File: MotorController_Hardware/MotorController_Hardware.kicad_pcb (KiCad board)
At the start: 2 copper layers, 124.5 x 150.9 mm, 243 parts, among them Q12 Q_NMOS_DGS, Q13 Q_NMOS_DGS, Q14 Q_NMOS_DGS, Q15 Q_NMOS_DGS, Q16 Q_NMOS_DGS, Q17 Q_NMOS_DGS, Q4 Q_NMOS_DGS, Q5 Q_NMOS_DGS, Q6 Q_NMOS_DGS, Q7 Q_NMOS_DGS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

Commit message: CDR Layout changes
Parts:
- added REF**: 4_40_Hole, MRDT_Drill_Holes:4_40_Hole_Corner, B.Cu at (58.6, -34.4)
- added REF**: 4_40_Hole, MRDT_Drill_Holes:4_40_Hole_Corner, B.Cu at (167.0, -34.4)
- D10, D11, D12, D16, D17, D18, D19, D20, D21, D7, D8, D9: value D_Zener -> 15V
- Q12, Q13, Q14, Q15, Q16, Q17, Q4, Q5, Q6, Q7, Q8, Q9: value Q_NMOS_DGS -> FQP30N06L
- R10, R81: value 2k -> 1.5K
- R14, R78: footprint Resistors_SMD:R_0603_HandSoldering -> Resistors_SMD:R_1206_HandSoldering
- U2, U6: moved to F.Cu
- U3: footprint MotorController_Hardware:LAUNCHXL_F28069M_Launchpad_FULL_Booster_SMD_Top -> MRDT_Shields:LAUNCHXL_F28069M_Launchpad_FULL_Booster_SMD_Bottom
- moved C37 57.7 mm to (54.9, -21.1), turned to 0 degrees
- moved C9 50.6 mm to (54.6, 0.25)
- moved C7 49.0 mm to (170.7, -18.5), turned to 180 degrees
- moved C45 48.7 mm to (170.9, 2.79)
- moved C5 43.3 mm to (157.2, -19.8), turned to 180 degrees
- moved C39 35.9 mm to (157.2, 1.52), turned to 180 degrees
- moved C38 33.5 mm to (68.3, -22.4), turned to 0 degrees
- moved C36 33.4 mm to (68.4, -1.02), turned to 0 degrees
- moved R69 24.8 mm to (119.5, -29.0), turned to 0 degrees
- moved R71 24.8 mm to (119.5, -7.62), turned to 0 degrees
- moved R73 24.8 mm to (119.5, 13.7), turned to 0 degrees
- moved R37 24.6 mm to (105.7, -34.5), turned to 180 degrees
- moved R67 24.6 mm to (105.7, 8.13), turned to 180 degrees
- moved R68 24.6 mm to (119.5, -39.6), turned to 0 degrees
- moved R70 24.6 mm to (119.5, -18.3), turned to 0 degrees
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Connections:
- C42 pad 1: +3V3 -> GND
- C42 pad 2: GND -> +3V3
- C65 pad 1: GND -> Net-(C65-Pad1)
- C65 pad 2: Net-(C65-Pad2) -> GND
- C66 pad 1: GND -> Net-(C66-Pad1)
- C66 pad 2: Net-(C66-Pad2) -> GND
- Conn1 pad 1: SL_TX_M1 -> SL_TX
- Conn1 pad 2: SL_RX_M1 -> SL_RX
- Conn1 pad 3: SL_TX_M2 -> (no net)
- Conn1 pad 4: SL_RX_M2 -> (no net)
- D33 pad 2: SL_TX_M1 -> (no net)
- D34 pad 2: SL_RX_M1 -> (no net)
- D35 pad 2: SL_TX_M2 -> (no net)
- D36 pad 2: SL_RX_M2 -> (no net)
- Q12 pad 1: PVDD_M2 -> MGH_A_M2
- Q12 pad 2: MGH_A_M2 -> PVDD_M2
- Q13 pad 1: SH_A_M2 -> MGL_A_M2
- Q13 pad 2: MGL_A_M2 -> SH_A_M2
- Q14 pad 1: PVDD_M2 -> MGH_B_M2
- Q14 pad 2: MGH_B_M2 -> PVDD_M2
- Q15 pad 1: SH_B_M2 -> MGL_B_M2
- Q15 pad 2: MGL_B_M2 -> SH_B_M2
- Q16 pad 1: PVDD_M2 -> MGH_C_M2
- Q16 pad 2: MGH_C_M2 -> PVDD_M2
- Q17 pad 1: SH_C_M2 -> MGL_C_M2
- Q17 pad 2: MGL_C_M2 -> SH_C_M2
- Q4 pad 1: PVDD_M1 -> MGH_A_M1
- Q4 pad 2: MGH_A_M1 -> PVDD_M1
- Q5 pad 1: SH_A_M1 -> MGL_A_M1
- Q5 pad 2: MGL_A_M1 -> SH_A_M1
- Q6 pad 1: PVDD_M1 -> MGH_B_M1
- Q6 pad 2: MGH_B_M1 -> PVDD_M1
- Q7 pad 1: SH_B_M1 -> MGL_B_M1
- Q7 pad 2: MGL_B_M1 -> SH_B_M1
- Q8 pad 1: PVDD_M1 -> MGH_C_M1
- Q8 pad 2: MGH_C_M1 -> PVDD_M1
- Q9 pad 1: SH_C_M1 -> MGL_C_M1
- Q9 pad 2: MGL_C_M1 -> SH_C_M1
- R49 pad 1: Net-(C66-Pad2) -> Net-(C65-Pad1)
- R49 pad 2: Net-(C65-Pad2) -> Net-(C66-Pad1)
- U3 pad P_10: INH_C_M2 -> (no net)
- U3 pad P_11: INL_C_M2 -> (no net)
- U3 pad P_15: UART_TX_M2 -> UART_RX
- U3 pad P_28: UART_TX_M1 -> UART_RX
- U3 pad P_29: UART_RX_M1 -> UART_TX
- U3 pad P_58: UART_RX_M2 -> UART_TX
- U3 pad P_6: INH_A_M2 -> (no net)
- U3 pad P_7: INL_A_M2 -> (no net)
- U3 pad P_8: INH_B_M2 -> (no net)
- U3 pad P_9: INL_B_M2 -> (no net)
- U4 pad 1: Net-(C44-Pad2) -> Net-(C44-Pad1)
- U4 pad 10: UART_TX_M1 -> UART_TX
- U4 pad 11: UART_TX_M2 -> (no net)
- U4 pad 12: UART_RX_M2 -> (no net)
- U4 pad 13: SL_RX_M2 -> (no net)
- U4 pad 14: SL_TX_M2 -> (no net)
- U4 pad 3: Net-(C44-Pad1) -> Net-(C44-Pad2)
- U4 pad 4: Net-(C43-Pad2) -> Net-(C43-Pad1)
- U4 pad 5: Net-(C43-Pad1) -> Net-(C43-Pad2)
- U4 pad 7: SL_TX_M1 -> SL_TX
- U4 pad 8: SL_RX_M1 -> SL_RX
- U4 pad 9: UART_RX_M1 -> UART_RX
- U5 pad 17: INH_A_M2 -> (no net)
- U5 pad 18: INL_A_M2 -> (no net)
- U5 pad 19: INH_B_M2 -> (no net)
- U5 pad 2: Net-(C65-Pad2) -> Net-(C65-Pad1)
- U5 pad 20: INL_B_M2 -> (no net)
- U5 pad 21: INH_C_M2 -> (no net)
- U5 pad 22: INL_C_M2 -> (no net)
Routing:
- net (no net): track 0.00 -> 400.2 mm, vias 0 -> 7
- net UART_RX: track 0.00 -> 123.5 mm, vias 0 -> 3
- net UART_TX_M2: track 122.5 -> 0.00 mm, vias 2 -> 0
- net UART_TX: track 0.00 -> 120.2 mm, vias 0 -> 3
- net UART_RX_M2: track 117.5 -> 0.00 mm, vias 2 -> 0
- net INL_C_M2: track 64.5 -> 0.00 mm
- net UART_TX_M1: track 60.2 -> 0.00 mm, vias 2 -> 0
- net INH_C_M2: track 60.1 -> 0.00 mm
- net UART_RX_M1: track 56.9 -> 0.00 mm, vias 2 -> 0
- net INL_B_M2: track 53.9 -> 0.00 mm
- net SL_TX_M2: track 49.5 -> 0.00 mm, vias 1 -> 0
- net INH_B_M2: track 49.0 -> 0.00 mm
- net SL_RX_M2: track 48.0 -> 0.00 mm, vias 1 -> 0
- net INL_A_M2: track 46.3 -> 0.00 mm
- net PVDD_M1: track 150.5 -> 109.0 mm
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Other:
- outline, holes or cut-outs redrawn

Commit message: silkscreen touchups
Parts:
- removed D35, D36: LED, LEDs:LED_0603_HandSoldering
- removed R76, R77: 500, Resistors_SMD:R_0603_HandSoldering
- removed TP1, TP10, TP11, TP12, TP2, TP21, TP22, TP23, TP24, TP25, TP26, TP27, TP28, TP29, TP3, TP4, TP5, TP6, TP7, TP8, TP9: TEST, Wire_Pads:SolderWirePad_single_1mmDrill
- added +3V3: TEST, Wire_Pads:SolderWirePad_single_1mmDrill, F.Cu at (125.2, 86.6)
- added G***: LOGO, MRDT_Silkscreens:Andrew_Van_Horn_Sig_15mm, F.Cu at (123.2, 101.3)
- added G***: LOGO, MRDT_Silkscreens:Shaun_McManus_Sig_15mm, F.Cu at (123.4, 97.8)
- added G***: LOGO, MRDT_Silkscreens:MRDT_Logo_20mm, F.Cu at (164.3, 96.3)
- added GHA_M1: tp, Wire_Pads:SolderWirePad_single_1mmDrill, F.Cu at (96.8, -23.9)
- added GHA_M2: TEST, Wire_Pads:SolderWirePad_single_1mmDrill, F.Cu at (128.3, -39.6)
- added GHB_M1: TEST, Wire_Pads:SolderWirePad_single_1mmDrill, F.Cu at (96.8, -2.54)
- added GHB_M2: TEST, Wire_Pads:SolderWirePad_single_1mmDrill, F.Cu at (128.3, -18.3)
- added GHC_M1: TEST, Wire_Pads:SolderWirePad_single_1mmDrill, F.Cu at (96.8, 18.8)
- added GHC_M2: TEST, Wire_Pads:SolderWirePad_single_1mmDrill, F.Cu at (128.3, 3.05)
- added GLA_M1: TEST, Wire_Pads:SolderWirePad_single_1mmDrill, F.Cu at (97.0, -34.5)
- added GLA_M2: TEST, Wire_Pads:SolderWirePad_single_1mmDrill, F.Cu at (128.3, -29.0)
- added GLB_M1: TEST, Wire_Pads:SolderWirePad_single_1mmDrill, F.Cu at (96.8, -13.2)
- added GLB_M2: TEST, Wire_Pads:SolderWirePad_single_1mmDrill, F.Cu at (128.3, -7.62)
- added GLC_M1: TEST, Wire_Pads:SolderWirePad_single_1mmDrill, F.Cu at (96.8, 8.13)
- added GLC_M2: TEST, Wire_Pads:SolderWirePad_single_1mmDrill, F.Cu at (128.3, 13.7)
- added PVDD_M1: TEST, Wire_Pads:SolderWirePad_single_1mmDrill, F.Cu at (81.7, 25.4)
- added PVDD_M2: TEST, Wire_Pads:SolderWirePad_single_1mmDrill, F.Cu at (144.0, 25.7)
- added SHA_M1: TEST, Wire_Pads:SolderWirePad_single_1mmDrill, F.Cu at (74.2, -32.0)
- added SHA_M2: TEST, Wire_Pads:SolderWirePad_single_1mmDrill, F.Cu at (151.4, -29.0)
- added SHB_M1: TEST, Wire_Pads:SolderWirePad_single_1mmDrill, F.Cu at (74.2, -10.7)
- added SHB_M2: TEST, Wire_Pads:SolderWirePad_single_1mmDrill, F.Cu at (151.1, -7.62)
- added SHC_M1: TEST, Wire_Pads:SolderWirePad_single_1mmDrill, F.Cu at (74.2, 10.7)
- added SHC_M2: TEST, Wire_Pads:SolderWirePad_single_1mmDrill, F.Cu at (151.1, 13.7)
- moved D4 11.5 mm to (121.6, 48.6), turned to 0 degrees
- moved R7 8.03 mm to (117.4, 48.6), turned to 0 degrees
- moved D34 2.81 mm to (60.0, 80.3)
- moved R75 2.81 mm to (55.5, 80.3)
- moved D33 1.53 mm to (60.2, 77.2)
- moved R74 1.53 mm to (55.7, 77.2)
- moved D26 0.25 mm to (101.0, 8.13)
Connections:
- D33 pad 2: (no net) -> SL_TX
- D34 pad 2: (no net) -> SL_RX
- U3 pad P_10: (no net) -> INH_C_M2
- U3 pad P_11: (no net) -> INL_C_M2
- U3 pad P_6: (no net) -> INH_A_M2
- U3 pad P_7: (no net) -> INL_A_M2
- U3 pad P_8: (no net) -> INH_B_M2
- U3 pad P_9: (no net) -> INL_B_M2
- U5 pad 17: (no net) -> INH_A_M2
- U5 pad 18: (no net) -> INL_A_M2
- U5 pad 19: (no net) -> INH_B_M2
- U5 pad 20: (no net) -> INL_B_M2
- U5 pad 21: (no net) -> INH_C_M2
- U5 pad 22: (no net) -> INL_C_M2
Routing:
- net (no net): track 400.2 -> 0.00 mm, vias 7 -> 0
- net INL_C_M2: track 0.00 -> 66.9 mm, vias 0 -> 1
- net INH_C_M2: track 0.00 -> 63.8 mm, vias 0 -> 1
- net INL_B_M2: track 0.00 -> 55.9 mm, vias 0 -> 1
- net INH_B_M2: track 0.00 -> 52.8 mm, vias 0 -> 1
- net INL_A_M2: track 0.00 -> 49.8 mm, vias 0 -> 1
- net INH_A_M2: track 0.00 -> 41.5 mm, vias 0 -> 1
- net NFAULT_M2: track 72.9 -> 84.4 mm, vias 1 -> 2
- net PVDDSENSE_M2: track 23.4 -> 31.9 mm, vias 1 -> 2
- net NOCTW_M2: track 61.5 -> 70.0 mm, vias 1 -> 2
- net CSENSE_M2: track 13.8 -> 21.8 mm, vias 1 -> 2
- net +3V3: track 76.9 -> 82.6 mm, vias 20 -> 21
- net SL_RX: track 38.8 -> 44.0 mm
- net PVDD_M2: track 144.0 -> 148.7 mm
- net BSENSE_M2: track 24.1 -> 28.7 mm, vias 1 -> 2
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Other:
- board text added: "+"
- board text added: "+3V3"
- board text added: "-"
- board text added: "4-40"
- board text added: "A1"
- board text added: "A2"
- board text added: "B1"
- board text added: "B2"
- board text added: "C1"
- board text added: "C2"
- board text added: "DRV 8301"
- board text added: "FAULT_M1"
- board text added: "GHA_M1"
- board text added: "GHA_M2"
- board text added: "GHB_M1"
- board text added: "GHB_M2"
- board text added: "GHC_M1"
- board text added: "GHC_M2"
- board text added: "GLA_M1"
- board text added: "GLA_M2"
- board text added: "GLB_M1"
- board text added: "GLB_M2"
- board text added: "GLC_M1"
- board text added: "GLC_M2"
- board text added: "OCTW_M1"
- board text added: "PVDD_M1"
- board text added: "Power"
- board text added: "R O V E S O H A R D"
- board text added: "RX"
- board text added: "TX"

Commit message: minor silkscreen changes
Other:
- board text added: "FAULT_M2"
- board text added: "OCTW_M2"
- board text added: "PVDD_M2"

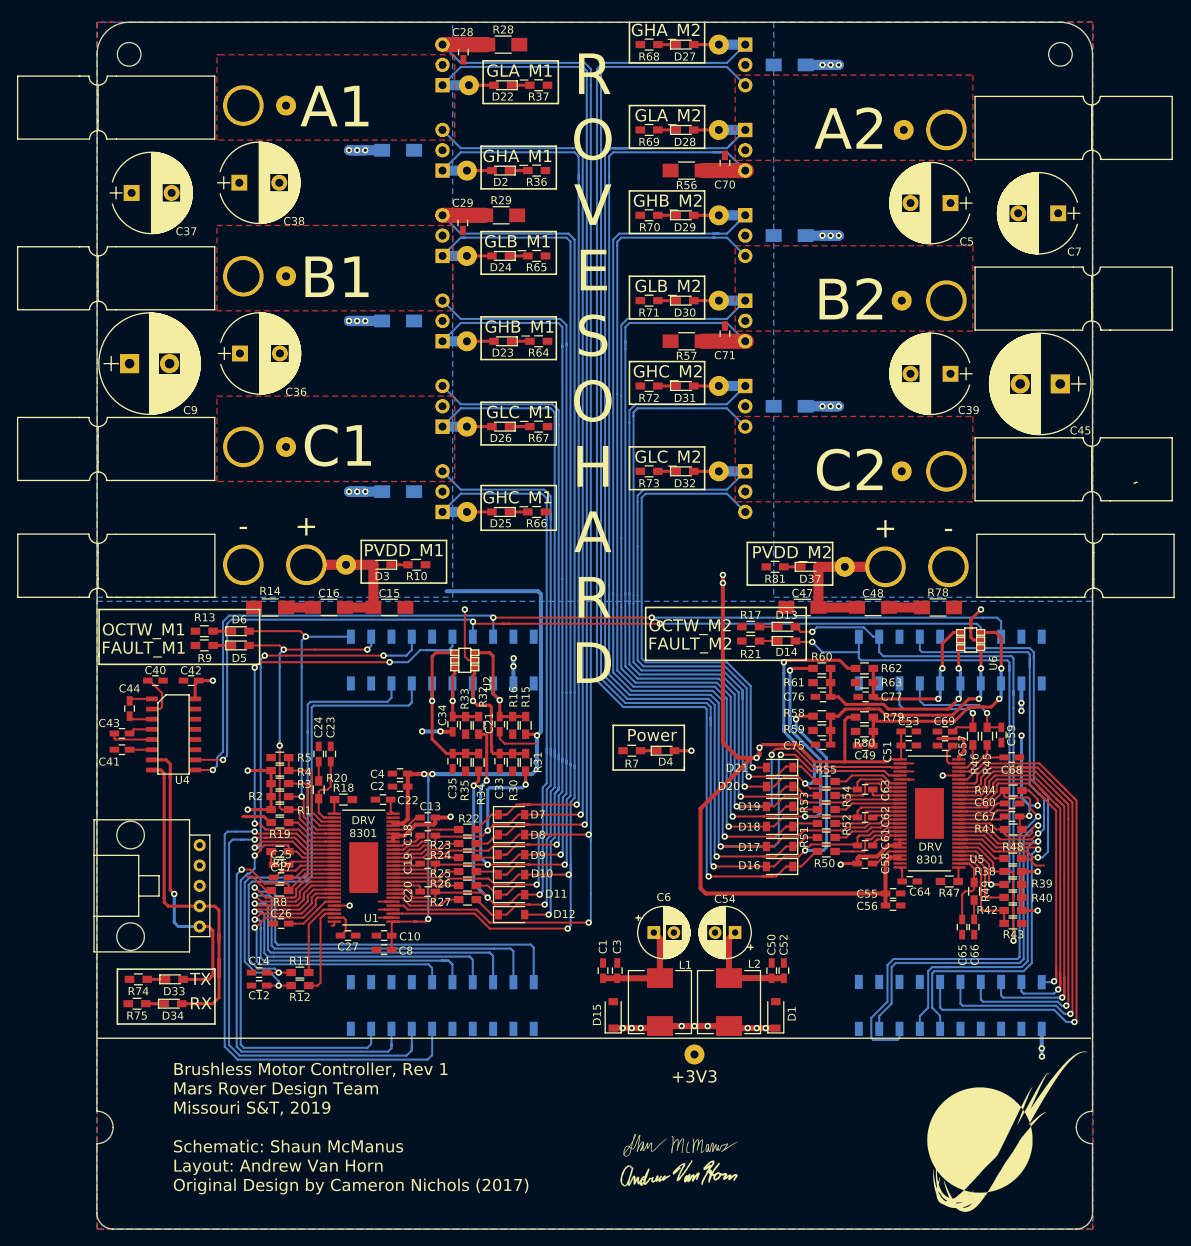
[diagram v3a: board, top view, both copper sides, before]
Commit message: fixed grounding
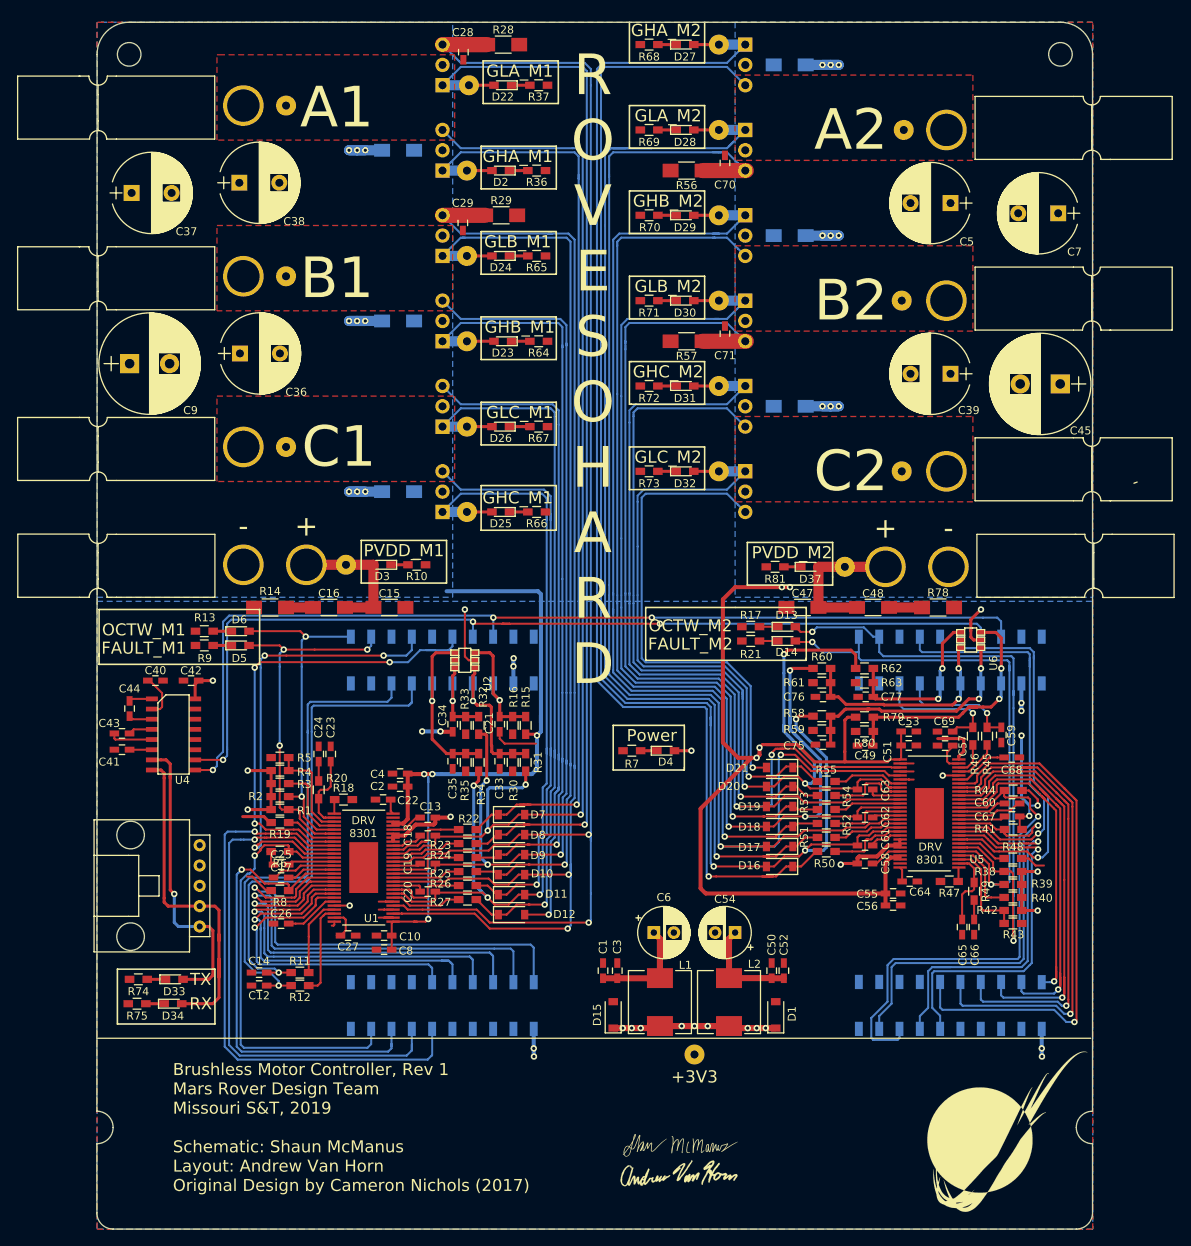
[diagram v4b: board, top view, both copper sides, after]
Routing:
- net PVDD_M2: track 148.7 -> 154.7 mm
- net GND: track 253.9 -> 257.3 mm, vias 31 -> 33
- net SH_C_M2: track 125.4 -> 128.0 mm
- net BSENSE_M2: track 28.7 -> 28.0 mm

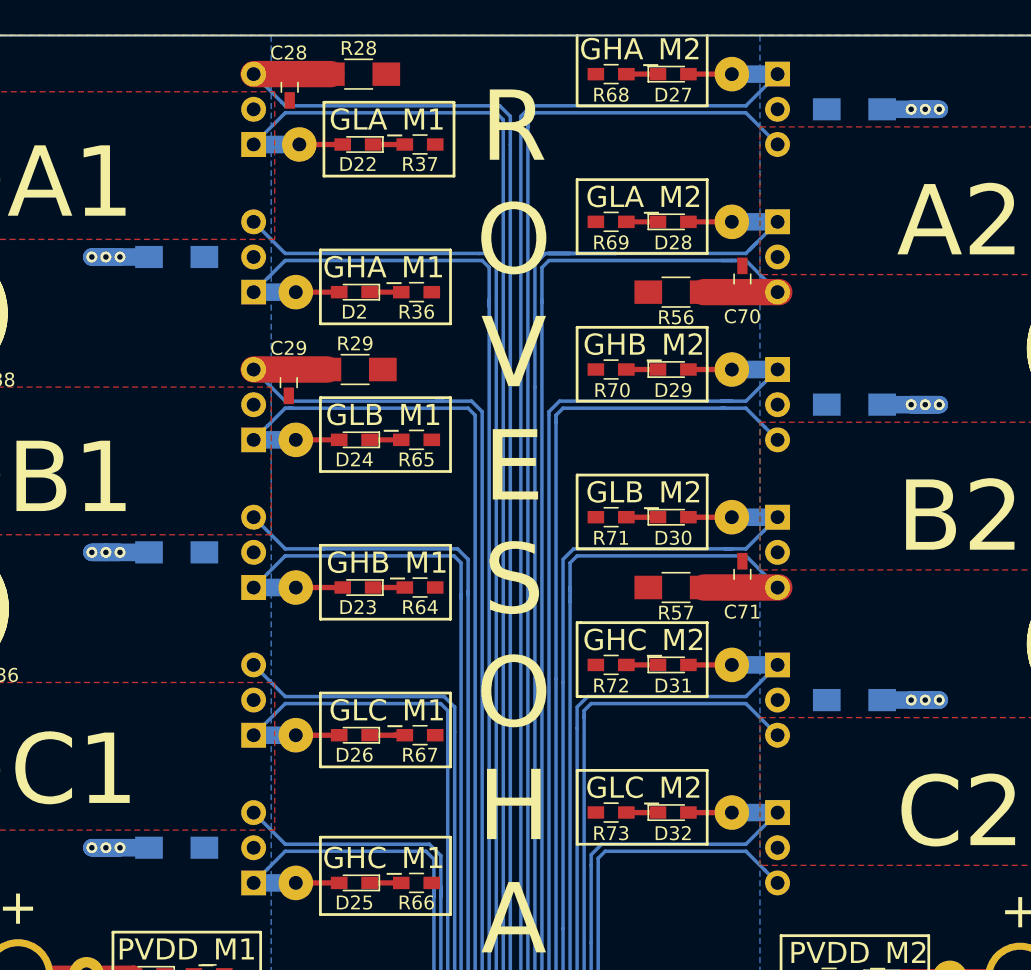
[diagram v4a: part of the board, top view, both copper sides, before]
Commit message: Moved PVDD caps to top layer
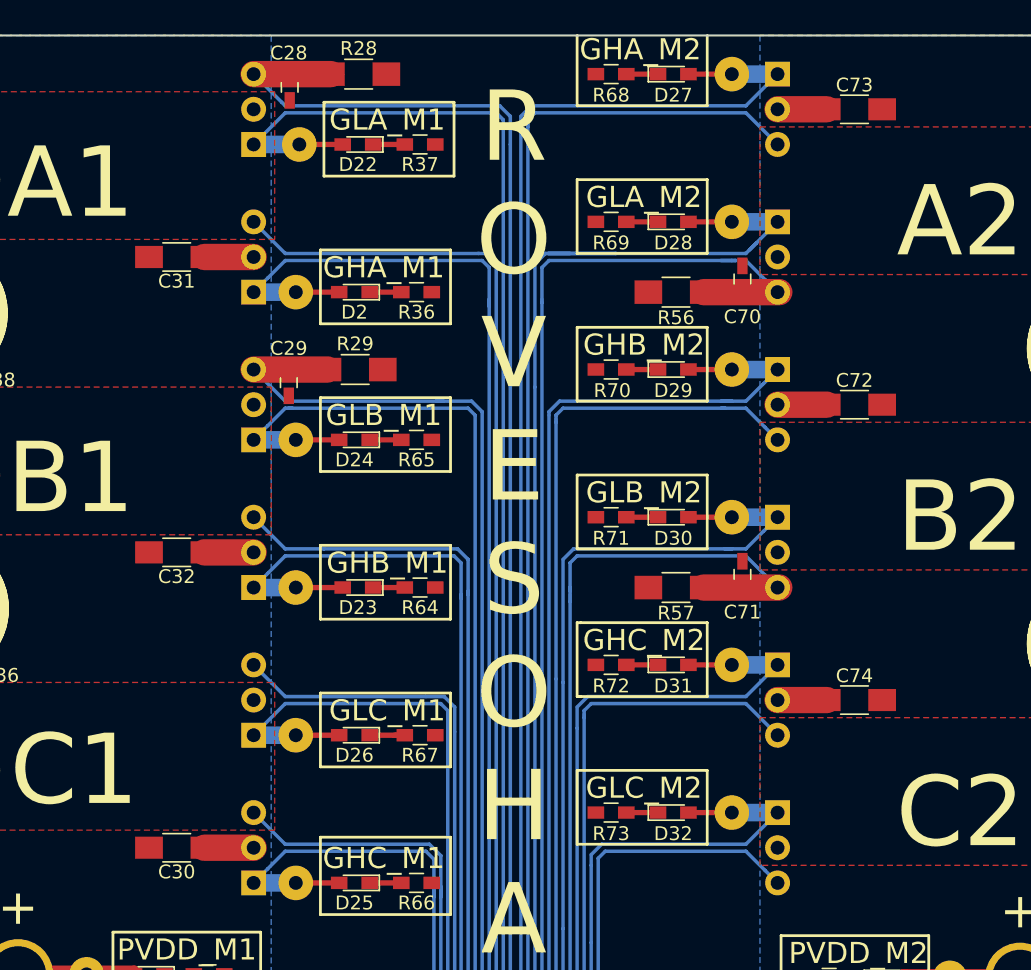
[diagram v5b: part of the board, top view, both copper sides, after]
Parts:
- C30, C31, C32, C72, C73, C74: moved to F.Cu
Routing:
- net GND: track 257.3 -> 220.4 mm, vias 33 -> 15
- net PVDD_M1: track 111.8 -> 122.5 mm
- net PVDD_M2: track 154.7 -> 165.4 mm

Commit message: Made lipinas changes
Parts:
- added REF**: 4_40_Hole, MRDT_Drill_Holes:4_40_Hole, B.Cu at (54.6, 18.3)
- added REF**: 4_40_Hole, MRDT_Drill_Holes:4_40_Hole, B.Cu at (170.9, 18.3)
- moved G*** 39.9 mm to (124.5, 97.2)
- moved G*** 20.3 mm to (103.1, 97.8)
- moved G*** 20.2 mm to (103.0, 100.5)
- moved C36 3.99 mm to (68.6, 2.97), turned to 90 degrees
- moved C38 3.74 mm to (68.6, -18.6), turned to 90 degrees
- moved C37 3.72 mm to (57.7, -18.6), turned to 90 degrees
- moved C9 3.55 mm to (56.9, 2.97), turned to 90 degrees
- moved C7 3.05 mm to (167.6, -18.6), turned to 90 degrees
- moved SHA_M2 2.81 mm to (151.1, -31.8)
- moved Conn11 2.79 mm to (160.3, 6.73)
- moved SHB_M2 2.79 mm to (151.1, -10.4)
- moved Conn10 2.79 mm to (160.3, -14.6)
- moved SHC_M2 2.79 mm to (151.1, 10.9)
- moved Conn9 2.79 mm to (160.3, -35.9)
- moved C45 2.56 mm to (168.4, 2.46), turned to 90 degrees
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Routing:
- net PVDD_M2: track 165.4 -> 160.6 mm
- net +3V3: track 82.6 -> 85.9 mm, vias 21 -> 23
- net GND: track 220.4 -> 222.6 mm, vias 15 -> 19
- net (no net): track 0.00 -> 2.03 mm, vias 0 -> 2
- net SH_B_M2: track 151.2 -> 151.7 mm
- added copper zone on F.Cu, net (none)
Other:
- board text added: "G"
- board text added: "Rx"
- board text added: "Serial"
- board text added: "TODAY TOMORROW FOREVER"
- board text added: "Tx"
